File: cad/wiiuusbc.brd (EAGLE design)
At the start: 12.1 x 11.2 mm, 3 parts, among them J1 USB4105-GF-A

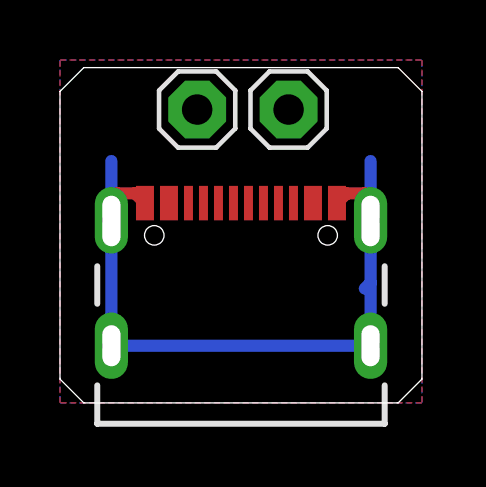
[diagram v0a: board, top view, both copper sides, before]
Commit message: connect CC lines and update readme
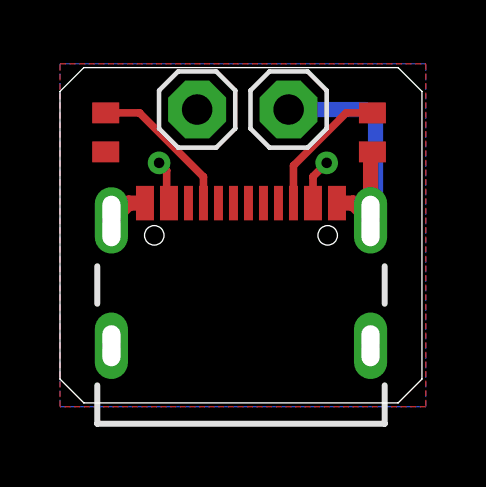
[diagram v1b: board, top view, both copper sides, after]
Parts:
- added R1, R2: 56K, adafruit:R0402
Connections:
- new net CC1: J1.A5, R1.2
- new net CC2: J1.B5, R2.1
- net GND: now also R1.1, R2.2
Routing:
- net GND: track 25.4 -> 11.4 mm
- net CC1: track 0.00 -> 5.02 mm
- net CC2: track 0.00 -> 4.61 mm
- net VCC: track 0.00 -> 3.01 mm, vias 0 -> 2
- added copper zone on layer 1, net GND
- added copper zone on layer 16, net VCC
- removed copper zone on layer 16, net GND
- removed copper zone on layer 1, net VCC
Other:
- board text added: "WiiU USB C"
- board text removed: "WiiU USB-C"
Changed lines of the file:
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@@
 <drawing>
 <settings>
-<setting alwaysvectorfont="yes"/>
+<setting alwaysvectorfont="no"/>
 <setting verticaltext="up"/>
 </settings>
-<grid distance="0.025" unitdist="inch" unit="inch" style="lines" multiple="1" display="yes" altdistance="5" altunitdist="mil" altunit="inch"/>
+<grid distance="0.01" unitdist="inch" unit="inch" style="lines" multiple="1" display="yes" altdistance="5" altunitdist="mil" altunit="inch"/>
 <layers>
 <layer number="1" name="Top" color="4" fill="1" visible="yes" active="yes"/>
@@
 <wire x1="0" y1="11.01725" x2="0.79375" y2="11.811" width="0" layer="20"/>
 <text x="6.0325" y="7.62" size="1.016" layer="26" font="vector" ratio="10" rot="MR0" align="center">WiiU
-USB-C</text>
+USB C</text>
 <text x="6.0325" y="3.81" size="1.016" layer="26" font="vector" ratio="10" rot="MR0" align="center">github.com/
 vaugerbird</text>
@@
 <attribute name="VALUE" x="3.302" y="7.239" size="1.27" layer="27"/>
 </element>
+<element name="R1" library="adafruit" package="R0402" value="56K" x="1.524" y="9.652" smashed="yes" rot="R90"/>
+<element name="R2" library="adafruit" package="R0402" value="56K" x="10.414" y="9.652" smashed="yes" rot="R270"/>
 </elements>
 <signals>
 <signal name="GND">
-<contactref element="J1" pad="A1_B12"/>
-<contactref element="J1" pad="B1_A12"/>
+<contactref element="R1" pad="1"/>
 <contactref element="J1" pad="S1"/>
 <contactref element="J1" pad="S2"/>
 <contactref element="J1" pad="S3"/>
 <contactref element="J1" pad="S4"/>
+<contactref element="J1" pad="A1_B12"/>
+<contactref element="J1" pad="B1_A12"/>
 <contactref element="JP1" pad="1"/>
-<polygon width="0.254" layer="16" spacing="0.4064">
-<vertex x="0" y="12.065"/>
-<vertex x="0" y="0.635"/>
-<vertex x="12.065" y="0.635"/>
-<vertex x="12.065" y="12.065"/>
+<polygon width="0.254" layer="1" isolate="0.254">
+<vertex x="0" y="11.938"/>
+<vertex x="12.192" y="11.938"/>
+<vertex x="12.192" y="0.508"/>
+<vertex x="0" y="0.508"/>
 </polygon>
-<wire x1="2.8325" y1="7.295" x2="2.5075" y2="7.62" width="0.4064" layer="1"/>
-<wire x1="2.5075" y1="7.62" x2="1.905" y2="7.62" width="0.4064" layer="1"/>
-<wire x1="1.905" y1="7.62" x2="1.5983" y2="7.3133" width="0.4064" layer="1"/>
-<wire x1="1.5983" y1="7.3133" x2="1.5983" y2="6.72" width="0.4064" layer="1"/>
-<wire x1="9.2325" y1="7.295" x2="9.525" y2="7.5875" width="0.4064" layer="1"/>
-<wire x1="9.525" y1="7.5875" x2="9.525" y2="7.62" width="0.4064" layer="1"/>
-<wire x1="9.525" y1="7.62" x2="10.16" y2="7.62" width="0.4064" layer="1"/>
-<wire x1="10.16" y1="7.62" x2="10.4667" y2="7.3133" width="0.4064" layer="1"/>
-<wire x1="10.4667" y1="7.3133" x2="10.4667" y2="6.72" width="0.4064" layer="1"/>
-<wire x1="1.7125" y1="6.72" x2="1.7125" y2="8.6975" width="0.4064" layer="16"/>
-<wire x1="10.3525" y1="6.72" x2="10.3525" y2="8.6975" width="0.4064" layer="16"/>
-<wire x1="10.3525" y1="6.72" x2="10.3525" y2="4.6375" width="0.4064" layer="16"/>
-<wire x1="10.3525" y1="4.6375" x2="10.16" y2="4.445" width="0.4064" layer="16"/>
-<wire x1="10.3525" y1="2.54" x2="10.3525" y2="4.6375" width="0.4064" layer="16"/>
-<wire x1="10.3525" y1="2.54" x2="1.7125" y2="2.54" width="0.4064" layer="16"/>
-<wire x1="1.7125" y1="2.54" x2="1.7125" y2="6.72" width="0.4064" layer="16"/>
-<wire x1="10.3525" y1="6.72" x2="10.4667" y2="6.72" width="0" layer="19" extent="1-1"/>
-<wire x1="1.5983" y1="6.72" x2="1.7125" y2="6.72" width="0" layer="19" extent="1-1"/>
+<contactref element="R2" pad="2"/>
+<wire x1="10.5175" y1="10.0565" x2="10.16" y2="10.414" width="0.508" layer="16"/>
+<wire x1="7.62" y1="10.414" x2="10.16" y2="10.414" width="0.508" layer="16"/>
+<wire x1="10.5175" y1="10.0565" x2="10.5175" y2="6.72" width="0.508" layer="16"/>
+<wire x1="9.2325" y1="7.295" x2="9.7775" y2="7.295" width="0.508" layer="1"/>
+<wire x1="9.7775" y1="7.295" x2="10.3525" y2="6.72" width="0.508" layer="1"/>
+<wire x1="10.3525" y1="6.72" x2="10.3525" y2="8.9405" width="0.508" layer="1"/>
+<wire x1="10.3525" y1="8.9405" x2="10.414" y2="9.002" width="0.508" layer="1"/>
+<wire x1="2.8325" y1="7.295" x2="2.2875" y2="7.295" width="0.508" layer="1"/>
+<wire x1="2.2875" y1="7.295" x2="1.7125" y2="6.72" width="0.508" layer="1"/>
+<wire x1="10.3525" y1="6.72" x2="10.5175" y2="6.72" width="0" layer="19" extent="16-16"/>
+</signal>
+<signal name="CC1">
+<contactref element="J1" pad="A5"/>
+<contactref element="R1" pad="2"/>
+<wire x1="1.524" y1="10.302" x2="2.652" y2="10.302" width="0.254" layer="1"/>
+<wire x1="4.7825" y1="8.1715" x2="4.7825" y2="7.295" width="0.254" layer="1"/>
+<wire x1="2.652" y1="10.302" x2="4.7825" y2="8.1715" width="0.254" layer="1"/>
+</signal>
+<signal name="CC2">
+<contactref element="J1" pad="B5"/>
+<contactref element="R2" pad="1"/>
+<wire x1="7.7825" y1="7.295" x2="7.7825" y2="8.5445" width="0.254" layer="1"/>
+<wire x1="9.54" y1="10.302" x2="10.414" y2="10.302" width="0.254" layer="1"/>
+<wire x1="7.7825" y1="8.5445" x2="9.54" y2="10.302" width="0.254" layer="1"/>
 </signal>
 <signal name="VCC">
@@
 <contactref element="J1" pad="B4_A9"/>
 <contactref element="JP2" pad="1"/>
-<polygon width="0.254" layer="1" spacing="0.4064">
-<vertex x="0" y="12.065"/>
-<vertex x="12.065" y="12.065"/>
-<vertex x="12.065" y="0.635"/>
-<vertex x="0" y="0.635"/>
+<polygon width="0.254" layer="16" isolate="0.254">
+<vertex x="0" y="11.938"/>
+<vertex x="0" y="0.508"/>
+<vertex x="12.192" y="0.508"/>
+<vertex x="12.192" y="11.938"/>
 </polygon>
+<wire x1="3.6325" y1="7.295" x2="3.556" y2="7.3715" width="0.254" layer="1"/>
+<wire x1="3.556" y1="7.3715" x2="3.556" y2="8.382" width="0.254" layer="1"/>
+<wire x1="3.556" y1="8.382" x2="3.302" y2="8.636" width="0.254" layer="1"/>
+<via x="3.302" y="8.636" extent="1-16" drill="0.35" shape="octagon"/>
+<wire x1="8.4325" y1="7.295" x2="8.4325" y2="8.1785" width="0.254" layer="1"/>
+<wire x1="8.4325" y1="8.1785" x2="8.89" y2="8.636" width="0.254" layer="1"/>
+<via x="8.89" y="8.636" extent="1-16" drill="0.35" shape="octagon"/>
 </signal>
 </signals>
